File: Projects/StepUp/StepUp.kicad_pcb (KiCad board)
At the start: 4 copper layers, 101 x 81 mm, 143 parts, among them J1 USB_C_Receptacle_USB2.0_16P, J10 Conn_01x02, J11 Conn_01x02, J12 Conn_01x02, J13 Conn_01x02, J14 Conn_01x02, J15 Conn_02x03_Counter_Clockwise, J2 Conn_01x02, J3 Conn_02x03_Counter_Clockwise, J4 Conn_02x05_Counter_Clockwise, J5 Conn_01x01_Pin, J6 Conn_01x01_Pin, J7 TBLH10-350-04BK, J8 Conn_01x01_Pin, J9 Conn_01x01_Pin, Q1 BSS84, Q2 2N7002, Q3 BSS83P, Q4 BSS83P, SW1 SW_Push, SW2 SW_Push, SW3 SW_Push, U1 USBLC6-2SC6, U2 W25Q128JVS, U3 RP2040, U4 TMC2300-LA, U5 NCP1117-3.3_SOT223, U6 MCP73832T-2ACI_OT, U7 MIC2253, Y1 ABM8-272-T3

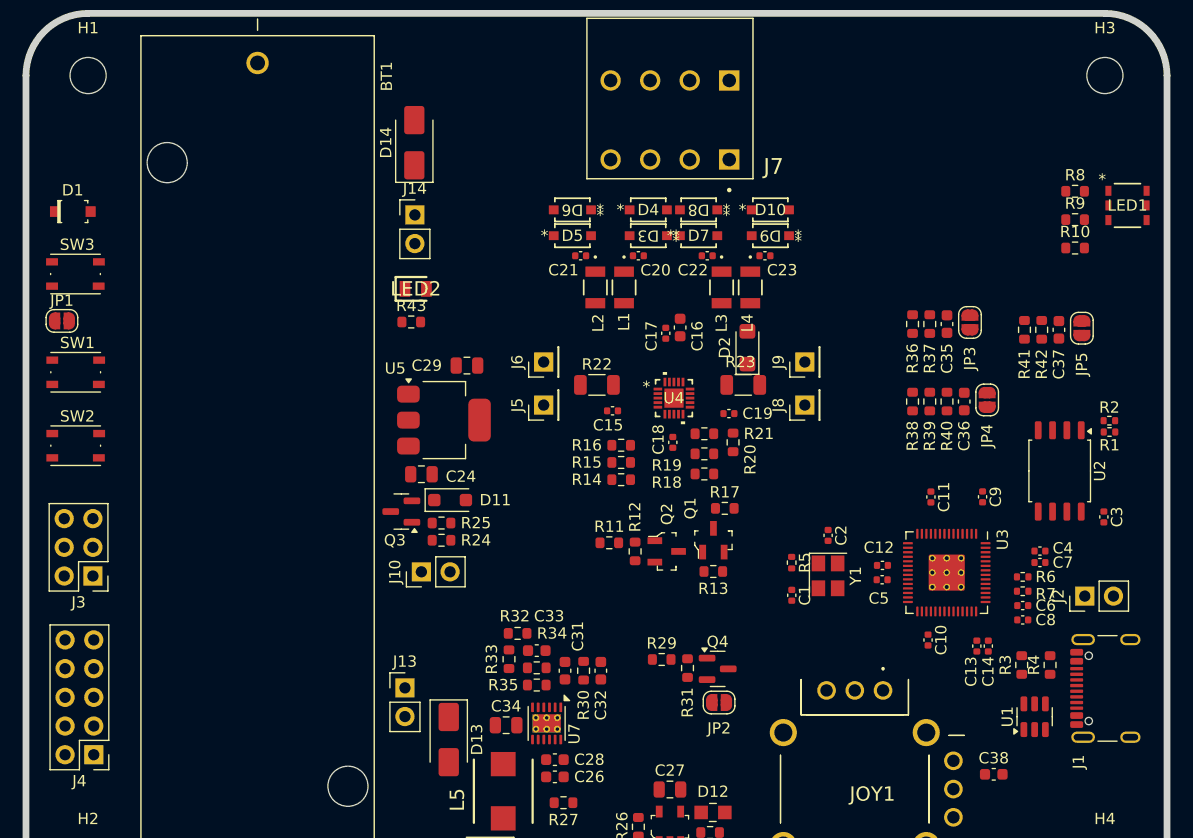
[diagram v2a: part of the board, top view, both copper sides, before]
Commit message: feat(tidy): Bigger PMOS, added footprints
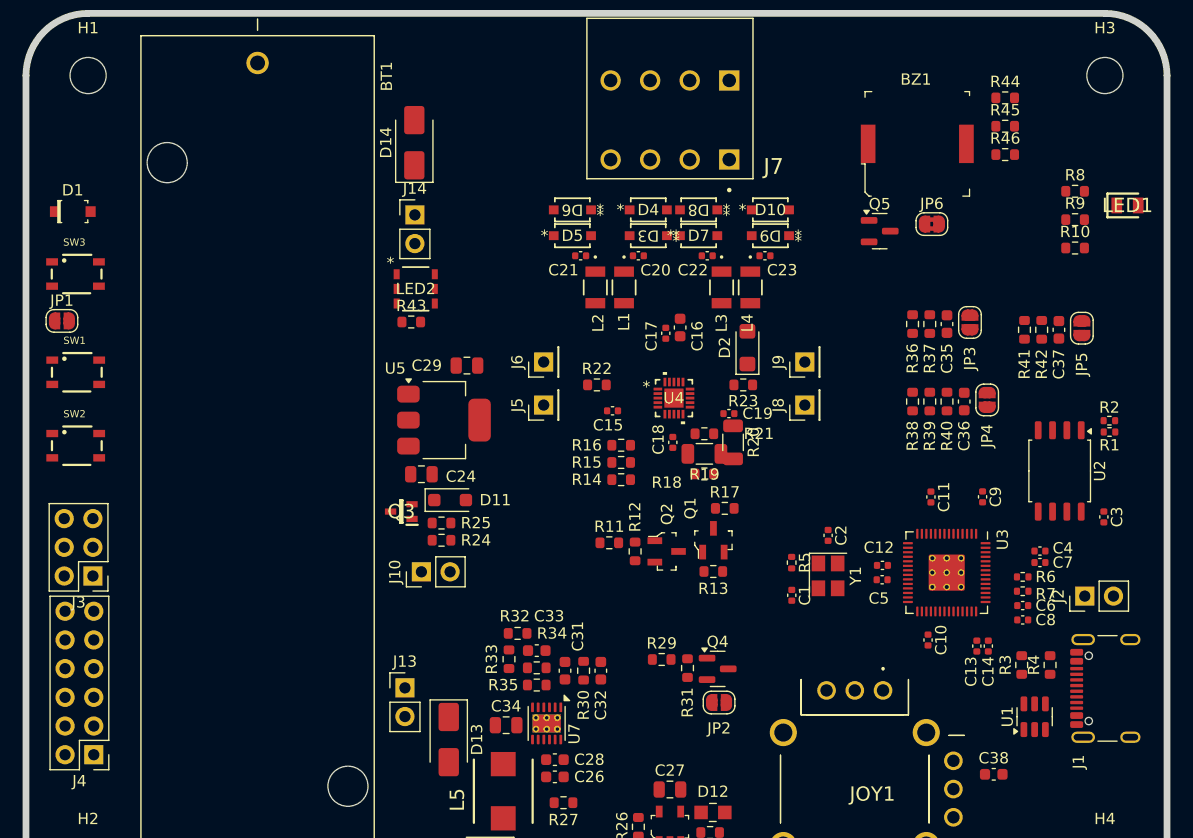
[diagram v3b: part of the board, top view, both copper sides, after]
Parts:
- added BZ1: PKMCS0909E4000-R1, digikey-footprints:Piezo_9x9mm_PKMCS0909E4000-R1, F.Cu at (163.4, 76.0)
- added JP6: SolderJumper_2_Bridged, Jumper:SolderJumper-2_P1.3mm_Bridged2Bar_RoundedPad1.0x1.5mm, F.Cu at (164.7, 83.2)
- added Q5: BSS83P, Package_TO_SOT_SMD:SOT-23, F.Cu at (160.1, 83.8)
- added R44: 1kR, Resistor_SMD:R_0603_1608Metric, F.Cu at (171.2, 72.0)
- added R45: 100kR, Resistor_SMD:R_0603_1608Metric, F.Cu at (171.2, 74.5)
- added R46: 1kR, Resistor_SMD:R_0603_1608Metric, F.Cu at (171.2, 77.0)
- J15, J3: value Conn_02x03_Counter_Clockwise -> Conn_02x03_Odd_Even
- J4: value Conn_02x05_Counter_Clockwise -> Conn_02x06_Odd_Even; footprint Connector_PinHeader_2.54mm:PinHeader_2x05_P2.54mm_Vertical -> Connector_PinHeader_2.54mm:PinHeader_2x06_P2.54mm_Vertical
- LED1: value APF3236LSEEZGKQBKC -> LTST-C171GKT; footprint Snapeda:APF3236LSEEZGKQBKC_KNB -> Samacsys:LEDC2012X90N
- LED2: value LTST-C171GKT -> APF3236LSEEZGKQBKC; footprint Samacsys:LEDC2012X90N -> Snapeda:APF3236LSEEZGKQBKC_KNB
- Q3: value BSS83P -> PMF170XP,115; footprint Package_TO_SOT_SMD:SOT-23 -> Samacsys:SOT65P210X110-3N
- R10, R9: value 330R -> 10kR
- R11: value 100R -> 10kR
- R17: value 10kR -> 1kR
- R18, R33, R35, R39: value 10kR -> 100kR
- R19: value 10kR -> 150mR; footprint Resistor_SMD:R_0603_1608Metric -> Resistor_SMD:R_1206_3216Metric
- R20: value 1kR -> 150mR; footprint Resistor_SMD:R_0603_1608Metric -> Resistor_SMD:R_1206_3216Metric
- R22: value 150mR -> 100R; footprint Resistor_SMD:R_1206_3216Metric -> Resistor_SMD:R_0603_1608Metric
- R23: value 150mR -> 2kR; footprint Resistor_SMD:R_1206_3216Metric -> Resistor_SMD:R_0603_1608Metric
- R25: value 100R -> 620R
- R26: value 2kR -> 100R
- R27: value 100kR -> 620R
- R28: value 620R -> 100kR
- R29: value 100R -> 9.09kR
- R30: value 620R -> 10kR
- R31: value 100kR -> 71.5kR
- R32: value 9.09kR -> 10kR
- R34: value 71.5kR -> 100kR
- R36, R37: value 100kR -> 10kR
- R40: value 10kR -> 620R
- R41: value 100kR -> 750R
- R42: value 100kR -> 330R
- R43: value 620R -> 330R
- R8: value 750R -> 100R
- SW1, SW2, SW3: value SW_Push -> 434133025816; footprint Button_Switch_SMD:SW_Push_1P1T_NO_Vertical_Wuerth_434133025816 -> Snapeda:434133025816_434133025816
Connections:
- J15 pad 2: JOYSTSICK_AXIS_H -> +3V3
- J15 pad 3: JOYSTSICK_BUTTON -> JOYSTSICK_AXIS_H
- J15 pad 5: GND -> JOYSTSICK_BUTTON
- J15 pad 6: +3V3 -> GND
- J3 pad 2: /MCU/SWD -> /MCU/UART_0_TX
- J3 pad 3: GND -> /MCU/SWD
- J3 pad 4: GND -> /MCU/UART_0_RX
- J3 pad 5: /MCU/UART_0_RX -> GND
- J3 pad 6: /MCU/UART_0_TX -> GND
- J4 pad 10: /MCU/GPIO10 -> GND
- J4 pad 2: /MCU/GPIO7 -> /MCU/GPIO10
- J4 pad 3: /MCU/GPIO8 -> /MCU/GPIO7
- J4 pad 4: /MCU/GPIO9 -> /MCU/GPIO11
- J4 pad 5: /MCU/GPIO16 -> /MCU/GPIO8
- J4 pad 6: /MCU/GPIO17 -> /MCU/GPIO12
- J4 pad 7: /MCU/GPIO13 -> /MCU/GPIO9
- J4 pad 8: /MCU/GPIO12 -> /MCU/GPIO13
- J4 pad 9: /MCU/GPIO11 -> /MCU/GPIO16
- LED1 pad 2: GND -> Net-(LED1-A)
- LED2 pad 2: Net-(LED2-A) -> GND
- R10 pad 1: /MCU/LED_BLUE -> Net-(Q1-G)
- R10 pad 2: Net-(LED1-Pad6) -> +3V3
- R11 pad 1: ~{TMC_STBDY} -> TMC_EN
- R11 pad 2: Net-(Q2-G) -> GND
- R12 pad 1: Net-(Q2-G) -> TMC_STEP
- R13 pad 1: Net-(Q1-G) -> TMC_DIR
- R13 pad 2: +3V3 -> GND
- R14 pad 1: TMC_EN -> /Motor Driver/TMC_VCC_IO
- R15 pad 1: TMC_STEP -> /Motor Driver/TMC_VCC_IO
- R15 pad 2: GND -> /Motor Driver/TMC_MS2/AD1
- R16 pad 1: TMC_DIR -> /Motor Driver/TMC_VCC_IO
- R16 pad 2: GND -> /Motor Driver/TMC_MS1/AD0
- R17 pad 1: /Motor Driver/TMC_VCC_IO -> TMC_UART_RX
- R17 pad 2: GND -> TMC_UART_TX
- R18 pad 1: /Motor Driver/TMC_VCC_IO -> TMC_UART_RX
- R18 pad 2: /Motor Driver/TMC_MS2/AD1 -> GND
- R19 pad 1: /Motor Driver/TMC_VCC_IO -> GND
- R19 pad 2: /Motor Driver/TMC_MS1/AD0 -> /Motor Driver/BRA
- R20 pad 1: TMC_UART_RX -> GND
- R20 pad 2: TMC_UART_TX -> /Motor Driver/BRB
- R21 pad 1: TMC_UART_RX -> GND
- R21 pad 2: GND -> Net-(D11-A)
- R22 pad 1: GND -> Net-(D11-A)
- R22 pad 2: /Motor Driver/BRA -> Net-(Q3-G)
- R23 pad 2: /Motor Driver/BRB -> Net-(U6-PROG)
- R24 pad 2: Net-(D11-A) -> /Power/BOOST_ENABLE
- R25 pad 1: Net-(D11-A) -> Net-(U6-STAT)
- R25 pad 2: Net-(Q3-G) -> Net-(D12-Pad2)
- R26 pad 1: GND -> V_USB
- R26 pad 2: Net-(U6-PROG) -> Net-(Q4-G)
- R27 pad 1: GND -> Net-(U7-COMP)
- R27 pad 2: /Power/BOOST_ENABLE -> Net-(C32-Pad1)
- R28 pad 1: Net-(U6-STAT) -> GND
- R28 pad 2: Net-(D12-Pad2) -> Net-(Q4-G)
- R29 pad 1: V_USB -> Net-(U7-OVP)
- R29 pad 2: Net-(Q4-G) -> /Power/BOOST_VOUT
- R30 pad 1: Net-(U7-COMP) -> GND
- R30 pad 2: Net-(C32-Pad1) -> Net-(U7-OVP)
- R31 pad 1: GND -> Net-(U7-FB)
- R31 pad 2: Net-(Q4-G) -> /Power/BOOST_VOUT
- R32 pad 1: Net-(U7-OVP) -> GND
- R32 pad 2: /Power/BOOST_VOUT -> Net-(U7-FB)
- R33 pad 1: GND -> Net-(JP3-A)
- R33 pad 2: Net-(U7-OVP) -> Vbat
- R34 pad 1: Net-(U7-FB) -> GND
- R34 pad 2: /Power/BOOST_VOUT -> Net-(JP3-A)
- R35 pad 1: GND -> Net-(JP4-A)
- R35 pad 2: Net-(U7-FB) -> VMotor
- R36 pad 1: Net-(JP3-A) -> Net-(JP4-A)
- R36 pad 2: Vbat -> Net-(R36-Pad2)
- R37 pad 1: GND -> Net-(R36-Pad2)
- R37 pad 2: Net-(JP3-A) -> GND
- R38 pad 1: Net-(JP4-A) -> Net-(JP5-A)
- R38 pad 2: VMotor -> V_USB
- R39 pad 1: Net-(JP4-A) -> GND
- R39 pad 2: Net-(R39-Pad2) -> Net-(JP5-A)
- R40 pad 1: Net-(R39-Pad2) -> Net-(LED1-A)
- R40 pad 2: GND -> Vbat
- R41 pad 1: Net-(JP5-A) -> LED_RED
- R41 pad 2: V_USB -> Net-(LED2-Pad4)
- R42 pad 1: GND -> LED_GREEN
- R42 pad 2: Net-(JP5-A) -> Net-(LED2-Pad5)
- R43 pad 1: Net-(LED2-A) -> LED_BLUE
- R43 pad 2: Vbat -> Net-(LED2-Pad6)
- R8 pad 1: /MCU/LED_RED -> ~{TMC_STBDY}
- R8 pad 2: Net-(LED1-Pad4) -> Net-(Q2-G)
- R9 pad 1: /MCU/LED_GREEN -> Net-(Q2-G)
- R9 pad 2: Net-(LED1-Pad5) -> GND
- SW1 pad 1: GND -> /MCU/RUN
- SW2 pad 1: GND -> Net-(D1-PadK)
- SW3 pad 1: GND -> Net-(JP1-B)
- U3 pad 28: /MCU/GPIO17 -> BUZZER
- U3 pad 35: /MCU/LED_RED -> LED_RED
- U3 pad 36: /MCU/LED_GREEN -> LED_GREEN
- U3 pad 37: /MCU/LED_BLUE -> LED_BLUE

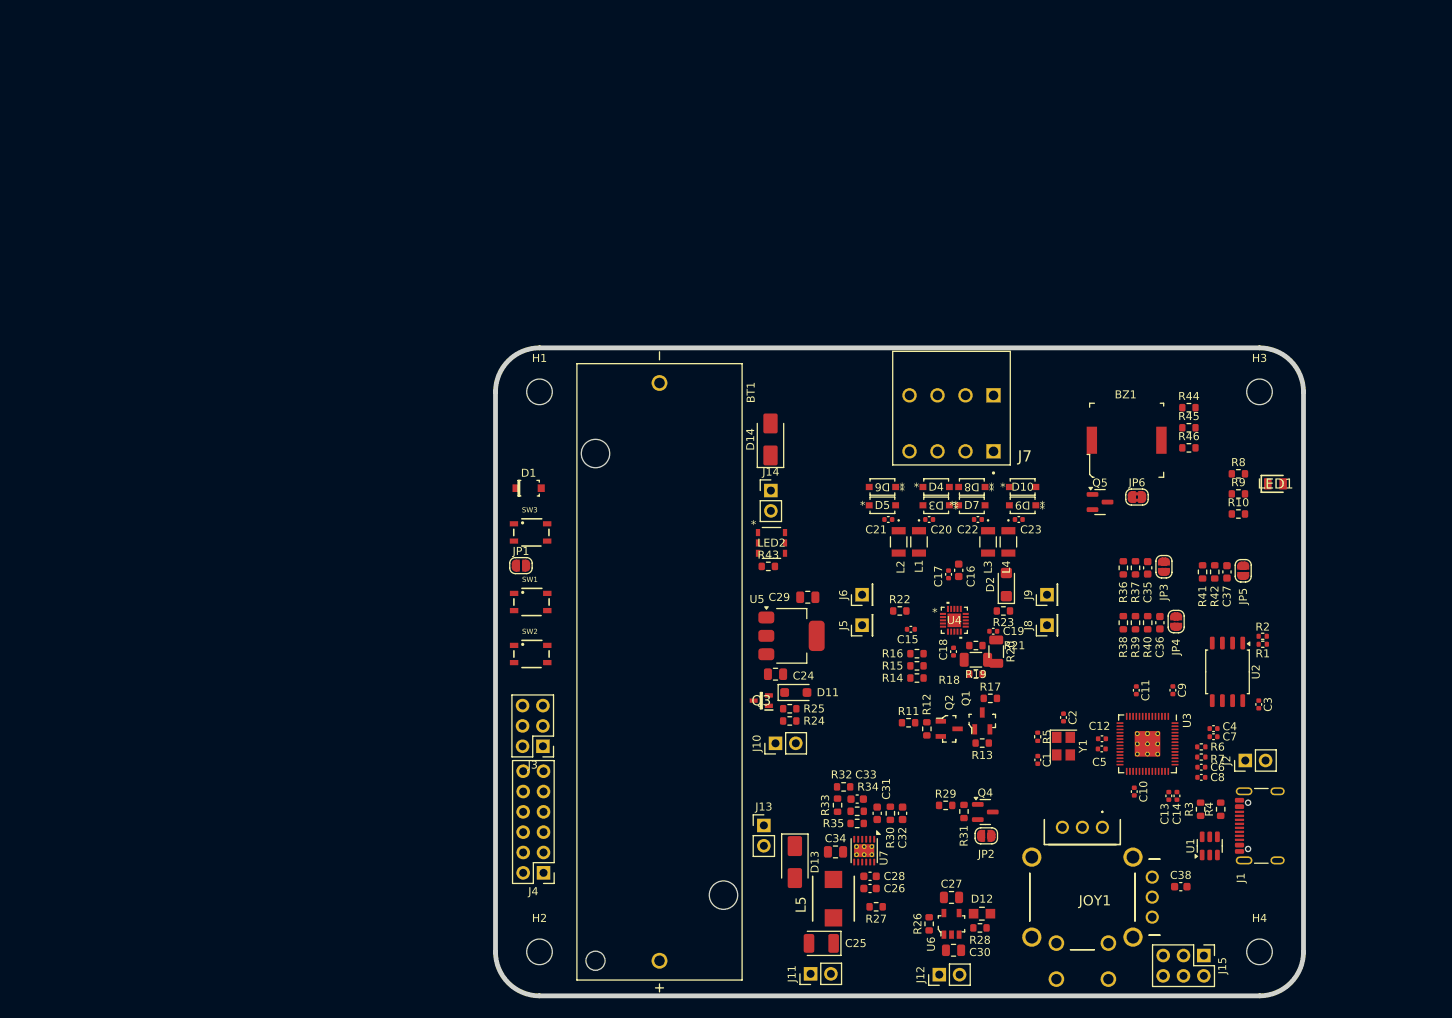
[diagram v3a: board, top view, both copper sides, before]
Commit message: feat(layout): TMC & Boost layout begin
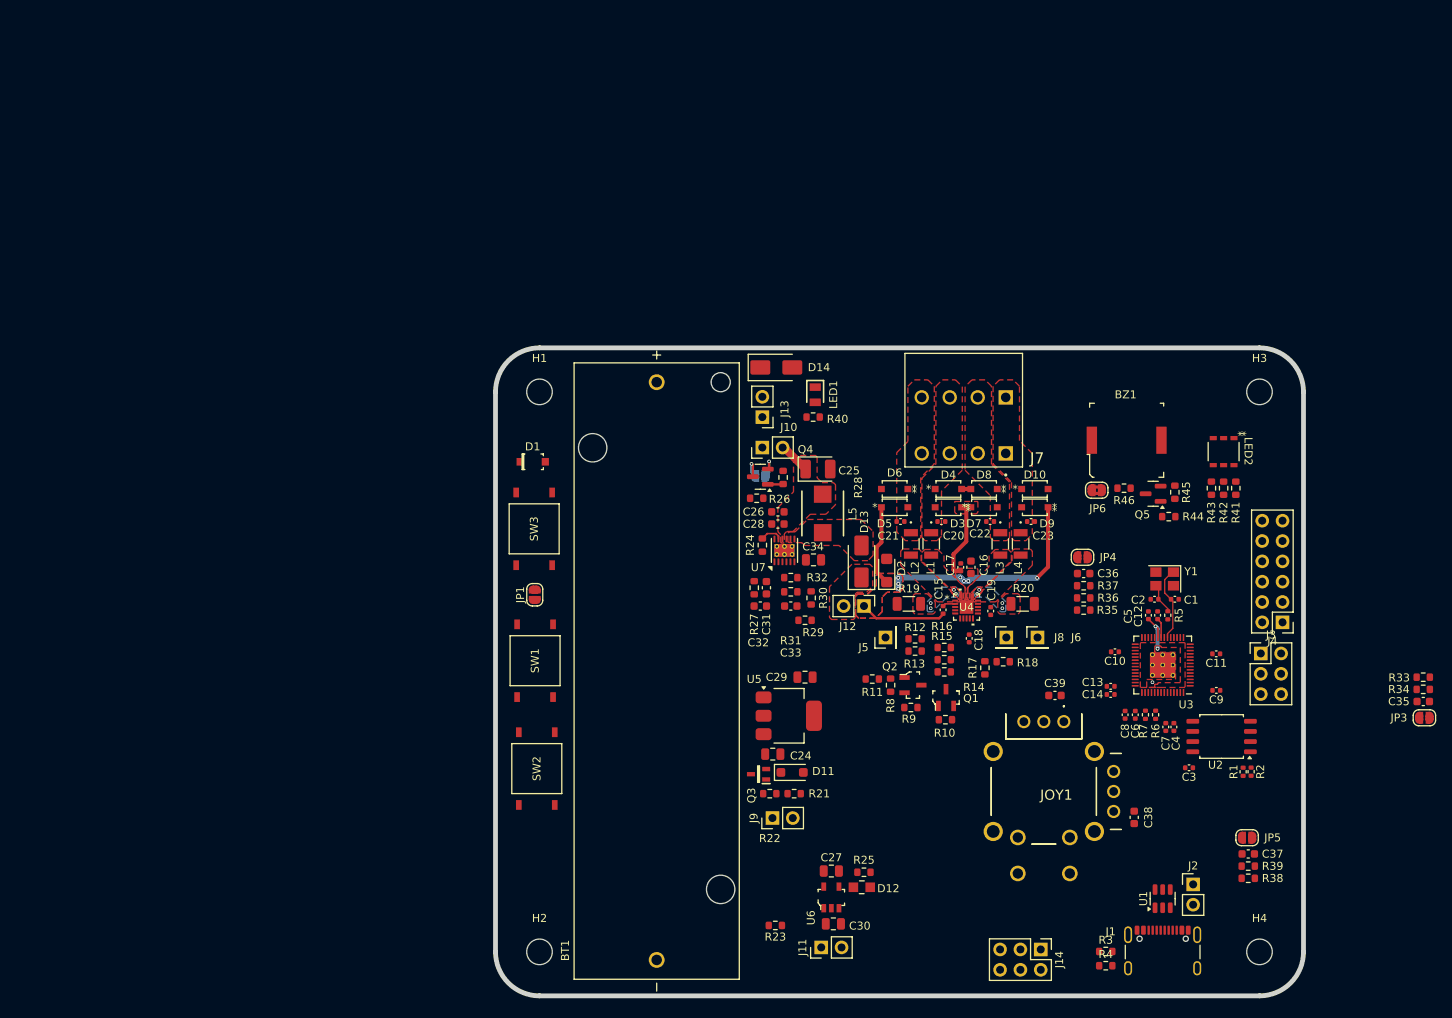
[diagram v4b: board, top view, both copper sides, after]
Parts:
- removed J15: Conn_02x03_Odd_Even, Connector_PinHeader_2.54mm:PinHeader_2x03_P2.54mm_Vertical
- added C39: 0.1uF, Capacitor_SMD:C_0603_1608Metric, F.Cu at (154.4, 108.0)
- J14: value Conn_01x02 -> Conn_02x03_Odd_Even; footprint Connector_PinHeader_2.54mm:PinHeader_1x02_P2.54mm_Vertical -> Connector_PinHeader_2.54mm:PinHeader_2x03_P2.54mm_Vertical
- J9: value Conn_01x01_Pin -> Conn_01x02; footprint Connector_PinHeader_2.54mm:PinHeader_1x01_P2.54mm_Vertical -> Connector_PinHeader_2.54mm:PinHeader_1x02_P2.54mm_Vertical
- JP2: moved to B.Cu
- SW1, SW2, SW3: value 434133025816 -> FSM8JSMASTR; footprint Snapeda:434133025816_434133025816 -> Snapeda:SW4_FSM8JSMASTR_TEC
- moved J4 97.5 mm to (182.9, 98.8)
- moved J3 90.5 mm to (180.2, 102.7), turned to 0 degrees
- moved R33 74.9 mm to (200.5, 105.7), turned to 180 degrees
- moved R34 72.4 mm to (200.5, 107.2), turned to 0 degrees
- moved J14 66.5 mm to (152.7, 139.7), turned to -90 degrees
- moved R28 61.4 mm to (120.5, 80.7), turned to -90 degrees
- moved C25 59.3 mm to (124.8, 79.7), turned to 0 degrees
- moved LED1 58.6 mm to (124.5, 70.4), turned to -90 degrees
- moved LED2 57.7 mm to (175.5, 77.5), turned to -90 degrees
- moved R26 57.4 mm to (117.2, 83.3), turned to 0 degrees
- moved R43 56.2 mm to (174.0, 82.0), turned to 90 degrees
- moved JP2 53.1 mm to (117.6, 80.5), turned to 180 degrees
- moved J13 51.0 mm to (117.9, 73.2), turned to 180 degrees
- moved R8 50.9 mm to (133.9, 106.7), turned to 90 degrees
- moved Q4 50.5 mm to (117.6, 80.6), turned to 180 degrees
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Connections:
- net /MCU/USB_D+ renamed USB_D+
- net /MCU/USB_D+_IN renamed USB_D+_IN
- net /MCU/USB_D- renamed USB_D-
- net /MCU/USB_D-_IN renamed USB_D-_IN
- net /Motor Driver/OA1 renamed OA1
- net /Motor Driver/OA1_OUT renamed OA1_OUT
- net /Motor Driver/OA2 renamed OA2
- net /Motor Driver/OA2_OUT renamed OA2_OUT
- net /Motor Driver/OB1 renamed OB1
- net /Motor Driver/OB1_OUT renamed OB1_OUT
- net /Motor Driver/OB2 renamed OB2
- net /Motor Driver/OB2_OUT renamed OB2_OUT
- C25 pad 1: /Power/BOOST_VIN -> BOOST_VIN
- C26 pad 1: /Power/BOOST_VIN -> BOOST_VIN
- C28 pad 1: /Power/BOOST_VIN -> BOOST_VIN
- C30 pad 1: Net-(J12-Pin_2) -> Net-(J11-Pin_2)
- C33 pad 1: /Power/BOOST_VOUT -> BOOST_VOUT
- C34 pad 1: /Power/BOOST_VOUT -> BOOST_VOUT
- D13 pad 1: /Power/BOOST_VOUT -> BOOST_VOUT
- J10 pad 1: V_USB -> Vbat
- J10 pad 2: Net-(D11-A) -> BOOST_VIN
- J11 pad 2: /Power/BOOST_VIN -> Net-(J11-Pin_2)
- J12 pad 1: Vbat -> VMotor
- J12 pad 2: Net-(J12-Pin_2) -> BOOST_VOUT
- J13 pad 1: VMotor -> Vbat
- J13 pad 2: /Power/BOOST_VOUT -> Net-(D14-K)
- J14 pad 1: Vbat -> JOYSTSICK_AXIS_V
- J14 pad 2: Net-(D14-K) -> +3V3
- J9 pad 1: GND -> V_USB
- L5 pad 1: /Power/BOOST_VIN -> BOOST_VIN
- R29 pad 2: /Power/BOOST_VOUT -> BOOST_VOUT
- R31 pad 2: /Power/BOOST_VOUT -> BOOST_VOUT
- U6 pad 3: Net-(J12-Pin_2) -> Net-(J11-Pin_2)
- U7 pad 10: /Power/BOOST_VIN -> BOOST_VIN
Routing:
- net VMotor: track 0.00 -> 60.6 mm, vias 0 -> 7
- net /MCU/XIN: track 0.00 -> 9.42 mm
- net /Power/BOOST_ENABLE: track 0.00 -> 5.80 mm, vias 0 -> 1
- net +1V1: track 0.00 -> 5.70 mm, vias 0 -> 3
- net BOOST_VIN: track 0.00 -> 3.98 mm
- net Net-(C2-Pad1): track 0.00 -> 3.82 mm
- net MCU_BOOST_EN: track 0.00 -> 3.52 mm, vias 0 -> 1
- net +3V3: track 0.00 -> 2.48 mm
- net Net-(Q4-G): track 0.00 -> 1.93 mm
- net Net-(U4-VCP): track 0.00 -> 1.62 mm
- net GND: track 0.00 -> 1.27 mm
- net /Motor Driver/BRB: vias 0 -> 4
- net /Motor Driver/BRA: vias 0 -> 4
- added copper zone on F.Cu, net +1V1
- added copper zone on F.Cu, net +3V3
- added copper zone on B.Cu, net /Motor Driver/BRA
- added copper zone on F.Cu, net /Motor Driver/BRA
- added copper zone on B.Cu, net /Motor Driver/BRB
- added copper zone on F.Cu, net /Motor Driver/BRB
- added copper zone on F.Cu, net BOOST_VIN
- added copper zone on F.Cu, net BOOST_VOUT
- added copper zone on In1.Cu, net GND
- added copper zone on In2.Cu, net GND
- added copper zone on F.Cu, net Net-(D13-A)
- added copper zone on F.Cu, net OA1
- added copper zone on F.Cu, net OA1_OUT
- added copper zone on F.Cu, net OA2
- added copper zone on F.Cu, net OA2_OUT
- added copper zone on F.Cu, net OB1
- added copper zone on F.Cu, net OB1_OUT
- added copper zone on F.Cu, net OB2
- added copper zone on F.Cu, net OB2_OUT
- added copper zone on B.Cu, net VMotor
- added copper zone on F.Cu, net VMotor
